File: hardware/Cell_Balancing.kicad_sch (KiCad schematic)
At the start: 16 parts

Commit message: updated sheets and 1st review changes
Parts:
- removed C105, C106, C107, C108, C109, C110, C111, C112: 0.47uF, symbol Device:C_Small
- removed R105, R107, R108, R109, R110, R111, R112, R113: 100, symbol Device:R_Small
- added C113, C135, C136, C137, C138, C139, C140, C141, C142: 0.47uF, symbol Device:C_Small
- added R106, R121, R122, R123, R124, R125, R126, R127: 8.2, symbol Device:R_Small
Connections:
- net AVSS: now also C113.2
- net BAT: now also R106.1
- net V0: now also R127.1
- net V1: now also R126.1
- net V2: now also R125.1
- net V3: now also R124.1
- net V4: now also R123.1
- net V5: now also R122.1
- net V6: now also R121.1
- new net CB0: C113.1, C142.2, R127.2
- new net CB1: C141.2, C142.1, R126.2
- new net CB2: C140.2, C141.1, R125.2
- new net CB3: C139.2, C140.1, R124.2
- new net CB4: C138.2, C139.1, R123.2
- new net CB5: C137.2, C138.1, R122.2
- new net CB6: C136.2, C137.1, R121.2
- new net CB7: C135.2, C136.1, R106.2
- new net preBAT: C135.1
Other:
- note added: "R_CB = ½ × (4.2V / 0.24A − 4.6Ω) = ½ × (17.5 − 4.6) = 6.45Ω ^ for 240mA balancing R_CB = ½ × (4.2V / 0.20A − 4.6Ω) = ½ × (21 − 4.6) = 8.2Ω ^ for 200mA balancing"

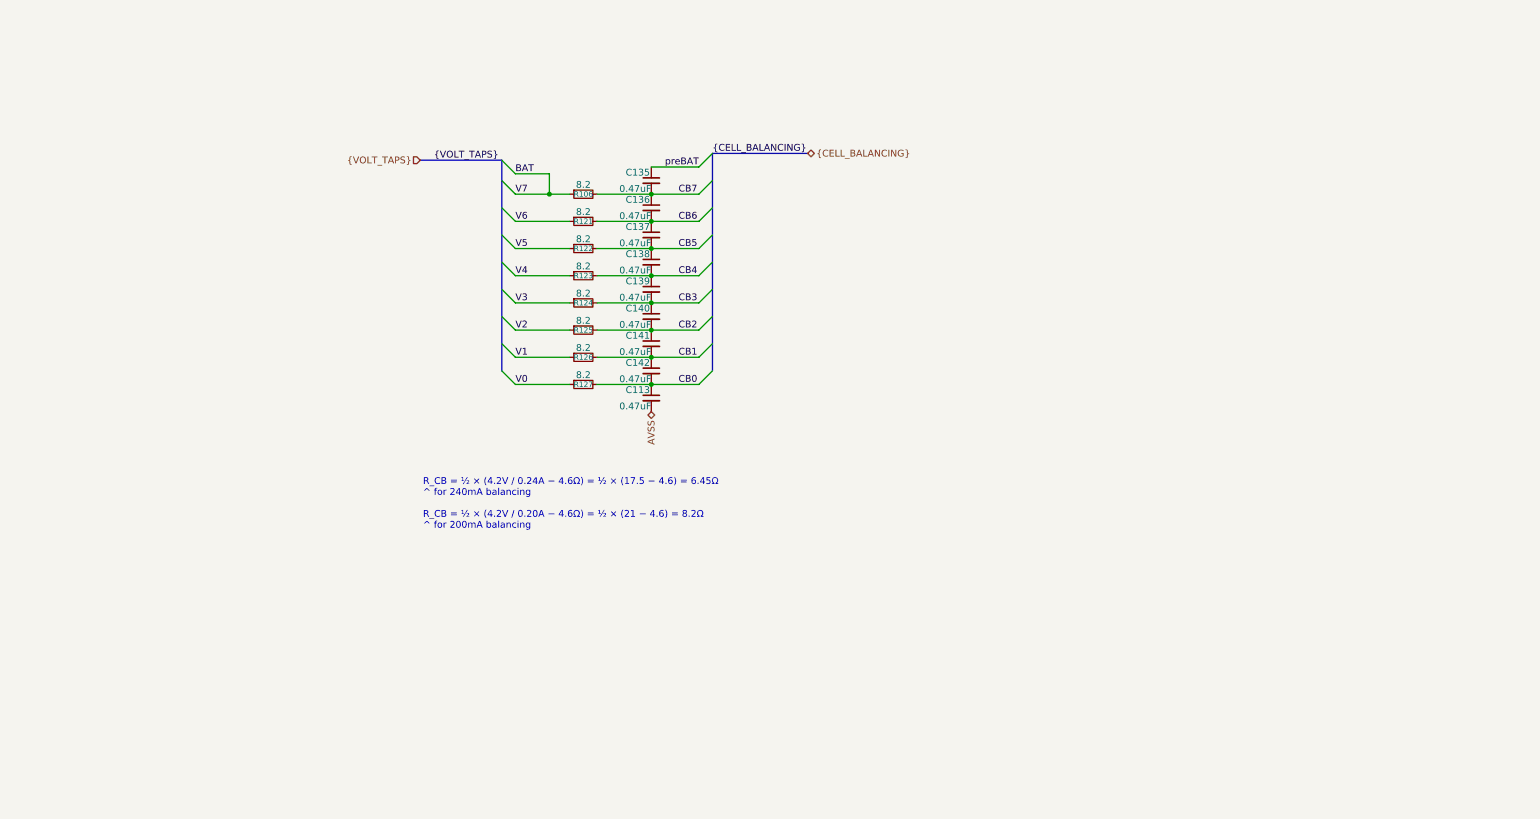
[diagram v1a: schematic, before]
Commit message: updated sheets, footprint, and calcs; 2nd review changes
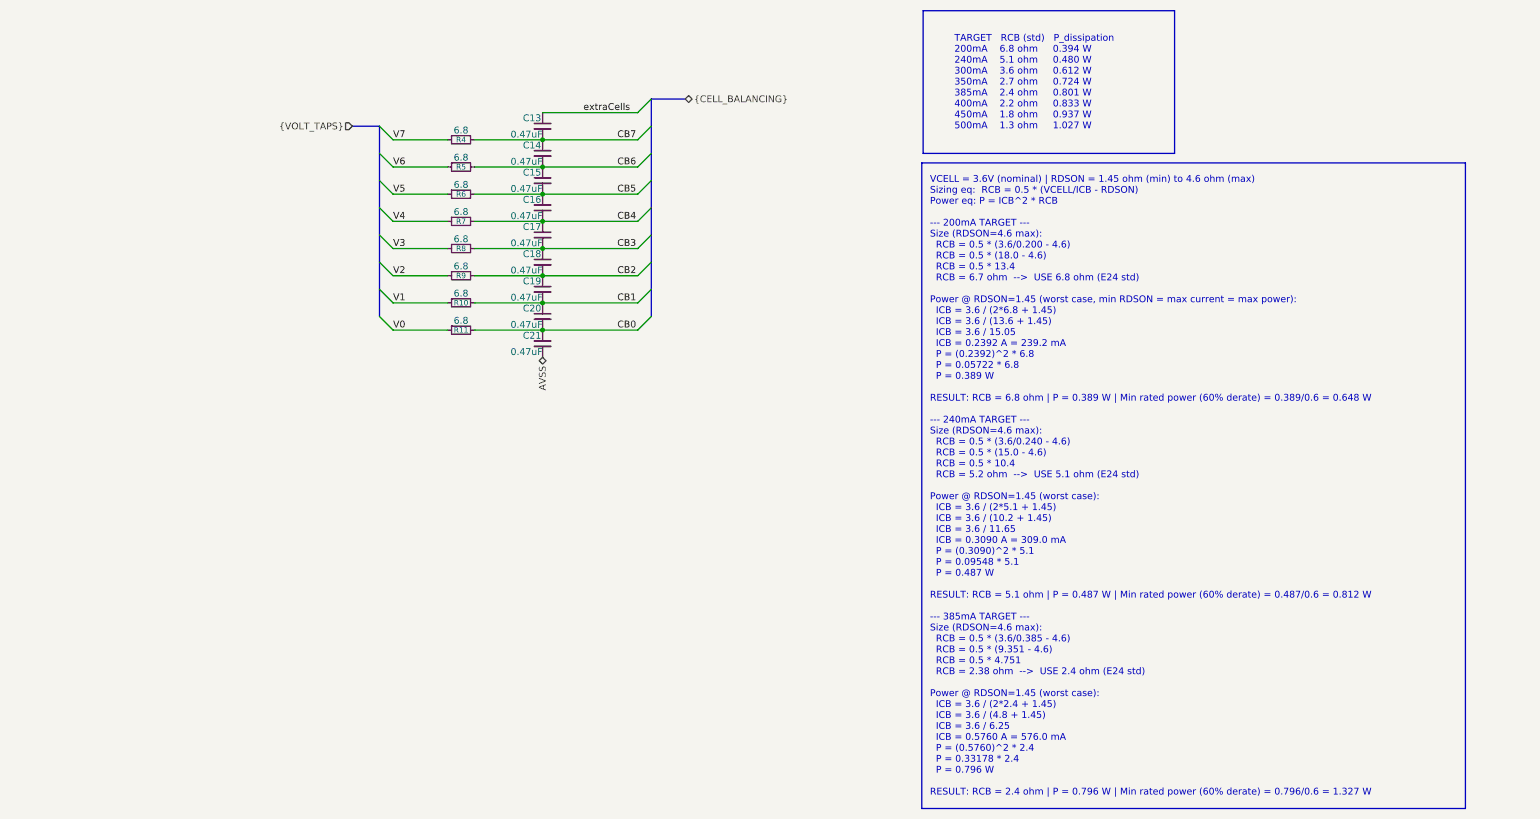
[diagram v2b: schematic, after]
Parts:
- C13: renamed from C135; footprint (none) -> Capacitor_SMD:C_0805_2012Metric_Pad1.18x1.45mm_HandSolder
- C14: renamed from C136; footprint (none) -> Capacitor_SMD:C_0805_2012Metric_Pad1.18x1.45mm_HandSolder
- C15: renamed from C137; footprint (none) -> Capacitor_SMD:C_0805_2012Metric_Pad1.18x1.45mm_HandSolder
- C16: renamed from C138; footprint (none) -> Capacitor_SMD:C_0805_2012Metric_Pad1.18x1.45mm_HandSolder
- C17: renamed from C139; footprint (none) -> Capacitor_SMD:C_0805_2012Metric_Pad1.18x1.45mm_HandSolder
- C18: renamed from C140; footprint (none) -> Capacitor_SMD:C_0805_2012Metric_Pad1.18x1.45mm_HandSolder
- C19: renamed from C141; footprint (none) -> Capacitor_SMD:C_0805_2012Metric_Pad1.18x1.45mm_HandSolder
- C20: renamed from C142; footprint (none) -> Capacitor_SMD:C_0805_2012Metric_Pad1.18x1.45mm_HandSolder
- C21: renamed from C113; footprint (none) -> Capacitor_SMD:C_0805_2012Metric_Pad1.18x1.45mm_HandSolder
- R10: renamed from R126; value 8.2 -> 6.8; footprint (none) -> Resistor_SMD:R_2512_6332Metric_Pad1.40x3.35mm_HandSolder
- R11: renamed from R127; value 8.2 -> 6.8; footprint (none) -> Resistor_SMD:R_2512_6332Metric_Pad1.40x3.35mm_HandSolder
- R4: renamed from R106; value 8.2 -> 6.8; footprint (none) -> Resistor_SMD:R_2512_6332Metric_Pad1.40x3.35mm_HandSolder
- R5: renamed from R121; value 8.2 -> 6.8; footprint (none) -> Resistor_SMD:R_2512_6332Metric_Pad1.40x3.35mm_HandSolder
- R6: renamed from R122; value 8.2 -> 6.8; footprint (none) -> Resistor_SMD:R_2512_6332Metric_Pad1.40x3.35mm_HandSolder
- R7: renamed from R123; value 8.2 -> 6.8; footprint (none) -> Resistor_SMD:R_2512_6332Metric_Pad1.40x3.35mm_HandSolder
- R8: renamed from R124; value 8.2 -> 6.8; footprint (none) -> Resistor_SMD:R_2512_6332Metric_Pad1.40x3.35mm_HandSolder
- R9: renamed from R125; value 8.2 -> 6.8; footprint (none) -> Resistor_SMD:R_2512_6332Metric_Pad1.40x3.35mm_HandSolder
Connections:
- net BAT renamed V7
- net preBAT renamed extraCells
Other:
- note added: "TARGET RCB (std) P_dissipation 200mA 6.8 ohm 0.394 W 240mA 5.1 ohm 0.480 W 300mA 3.6 ohm 0.612 W 350mA 2.7 ohm 0.724 W 385mA 2.4 ohm 0.801 W 400mA 2.2 ohm 0.833 W 450mA 1.8 ohm 0.937 W 500mA 1.3 ohm 1.027 W"
- note added: "VCELL = 3.6V (nominal) | RDSON = 1.45 ohm (min) to 4.6 ohm (max) Sizing eq: RCB = 0.5 * (VCELL/ICB - RDSON) Power eq: P = ICB^2 * RCB --- 200mA TARGET --- Size (RDSON=4.6 max): RCB = 0.5 * (3.6/0.200 - 4.6) RCB = 0.5 * (18.0 - 4.6) RCB = 0.5 * 13.4 RCB = 6.7 ohm --> USE 6.8 ohm (E24 std) Power @ RDSON=1.45 (worst case, min RDSON = max current = max power): ICB = 3.6 / (2*6.8 + 1.45) ICB = 3.6 / (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"
- note removed: "R_CB = ½ × (4.2V / 0.24A − 4.6Ω) = ½ × (17.5 − 4.6) = 6.45Ω ^ for 240mA balancing R_CB = ½ × (4.2V / 0.20A − 4.6Ω) = ½ × (21 − 4.6) = 8.2Ω ^ for 200mA balancing"
- moved on the sheet: C13, C14, C15, C16, C17, C18, C19, C20, C21, R10, R11, R4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
